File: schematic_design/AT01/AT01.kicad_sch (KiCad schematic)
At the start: 25 parts, among them J1 JST Connector, M2 Motor_DC (Pump), M3 Motor_DC (Solenoid), P1 USB_C_Plug_USB2.0, Q1 DMG2301L, SW1 SW_Push, U1 MPRLS0025PA00001A, U2 FT232RL, U3 DRV8833PW

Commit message: completed initial schematic development
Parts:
- added C7: 4.7uF, symbol Device:C
- added D2: LED, symbol Device:LED
- added J2: Conn_01x04_Pin, symbol Connector:Conn_01x04_Pin
- added R10, R5, R6, R7, R8, R9: 5.1K, symbol Device:R
- added U4: MCP73831-2-OT, Package_TO_SOT_SMD:SOT-23-5, symbol Battery_Management:MCP73831-2-OT
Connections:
- net +BATT: now also C7.2, U4.3 (V_{BAT})
- net GND: now also P1.A1 (GND), P1.A12 (GND), P1.B1 (GND), P1.B12 (GND), C7.1, D2.1 (K), R5.2, R8.2, R9.2, U4.2 (V_{SS})
- net IO32_A7: now also J2.4 (Pin_4)
- net MISO: now also J2.3 (Pin_3)
- net MOSI: now also J2.2 (Pin_2)
- net RXD0: now also U2.1 (TXD)
- net SCK: now also J2.1 (Pin_1)
- net TXD0: now also U2.5 (RXD)
- net VBUS: now also P1.A4 (VBUS), P1.A9 (VBUS), P1.B4 (VBUS), P1.B9 (VBUS), R6.1, R7.1, U4.4 (V_{DD})
- net DTR: now reaches U2.2 (DTR)
- net VBUS_UART: now reaches U2.20 (VCC), U2.4 (VCCIO)
- net VBUS_UART: now also R6.2, R7.2, R8.1
- net RTS: now reaches U2.3 (RTS)
- net at P1.A5 (CC): now also R5.1
- new net: D2.2 (A), R10.1
- new net: R10.2, U4.1 (STAT)
- new net: R9.1, U4.5 (PROG)
- no-connect marks 9 -> 18
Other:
- note added: "LIPO CHARGING CIRCUIT"
- note added: "SPI BREAKOUT HEADER"
- note added: "USB TO UART BRIDGE CIRCUIT"
- note removed: "2. add input circuit 3. add charging circuit 5. add usb to uart circuit"
- title: (none) -> AT01 - Initial Revision
- moved on the sheet: C6, P1, U2

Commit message: adding libs, cleaning up sch, initial pcb commit
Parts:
- removed R1, R2: 2.2k, symbol Device:R_Small_US
- added R12: 2.2K, Resistor_SMD:R_0402_1005Metric_Pad0.72x0.64mm_HandSolder, symbol Device:R
- added R13, R2: 10K, Resistor_SMD:R_0402_1005Metric_Pad0.72x0.64mm_HandSolder, symbol Device:R
- C1, C2, C3, C4, C5, C6, C7: footprint (none) -> Capacitor_SMD:C_01005_0402Metric_Pad0.57x0.30mm_HandSolder
- C8, C9: renamed from C?; footprint (none) -> Capacitor_SMD:C_01005_0402Metric_Pad0.57x0.30mm_HandSolder
- D2: footprint (none) -> LED_THT:LED_D3.0mm
- J1: footprint (none) -> Connector_JST:JST_EH_S2B-EH_1x02_P2.50mm_Horizontal
- J2: footprint (none) -> Connector_JST:JST_EH_S4B-EH_1x04_P2.50mm_Horizontal
- M2, M3: footprint (none) -> Connector_Samtec_HPM_THT:Samtec_HPM-02-05-x-S_Straight_1x02_Pitch5.08mm
- P1: footprint (none) -> Connector_USB:USB_C_Receptacle_Molex_105450-0101
- R10, R3, R4, R5, R6, R7, R8, R9: footprint (none) -> Resistor_SMD:R_0402_1005Metric_Pad0.72x0.64mm_HandSolder
- R11: renamed from R?; footprint (none) -> Resistor_SMD:R_0402_1005Metric_Pad0.72x0.64mm_HandSolder
- SW1: footprint (none) -> Button_Switch_THT:SW_PUSH_6mm
- gave numbers to parts that had none: 2
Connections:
- net IO27_A10 is gone; now on net DRV_SLEEP: U5.12 (IO27)
- net +3.3V: now also U1.12 (VDD), R13.1, R2.1; no longer U1.10 (VSS)
- net GND: now also C1.2, U1.10 (VSS), R12.1; no longer U3.3 (AISEN), U3.6 (BISEN)
- net SCK: now also U5.20 (SCK/CLK)
- net SCL: now also R2.2
- net SDA: now also R13.2
- net IO12_A11 renamed DRV_SLEEP
- new net: R12.2, U3.3 (AISEN), U3.6 (BISEN)
- no-connect marks 18 -> 37

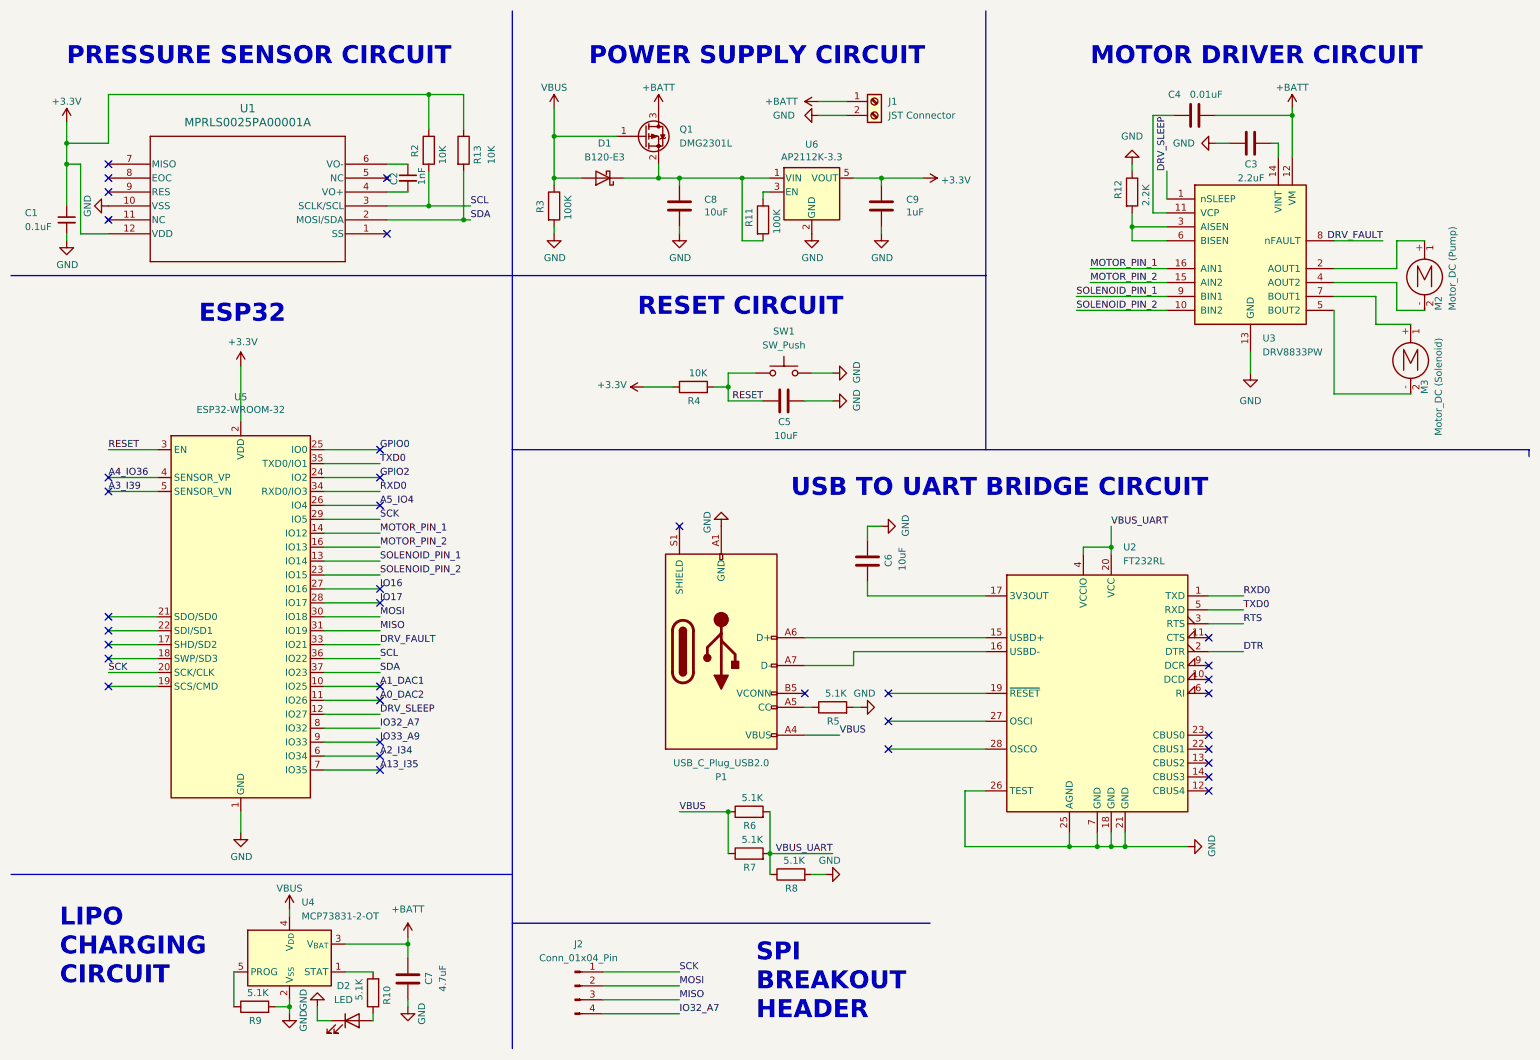
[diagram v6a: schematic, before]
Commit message: fixing up labels, gnds, added some protection diodes
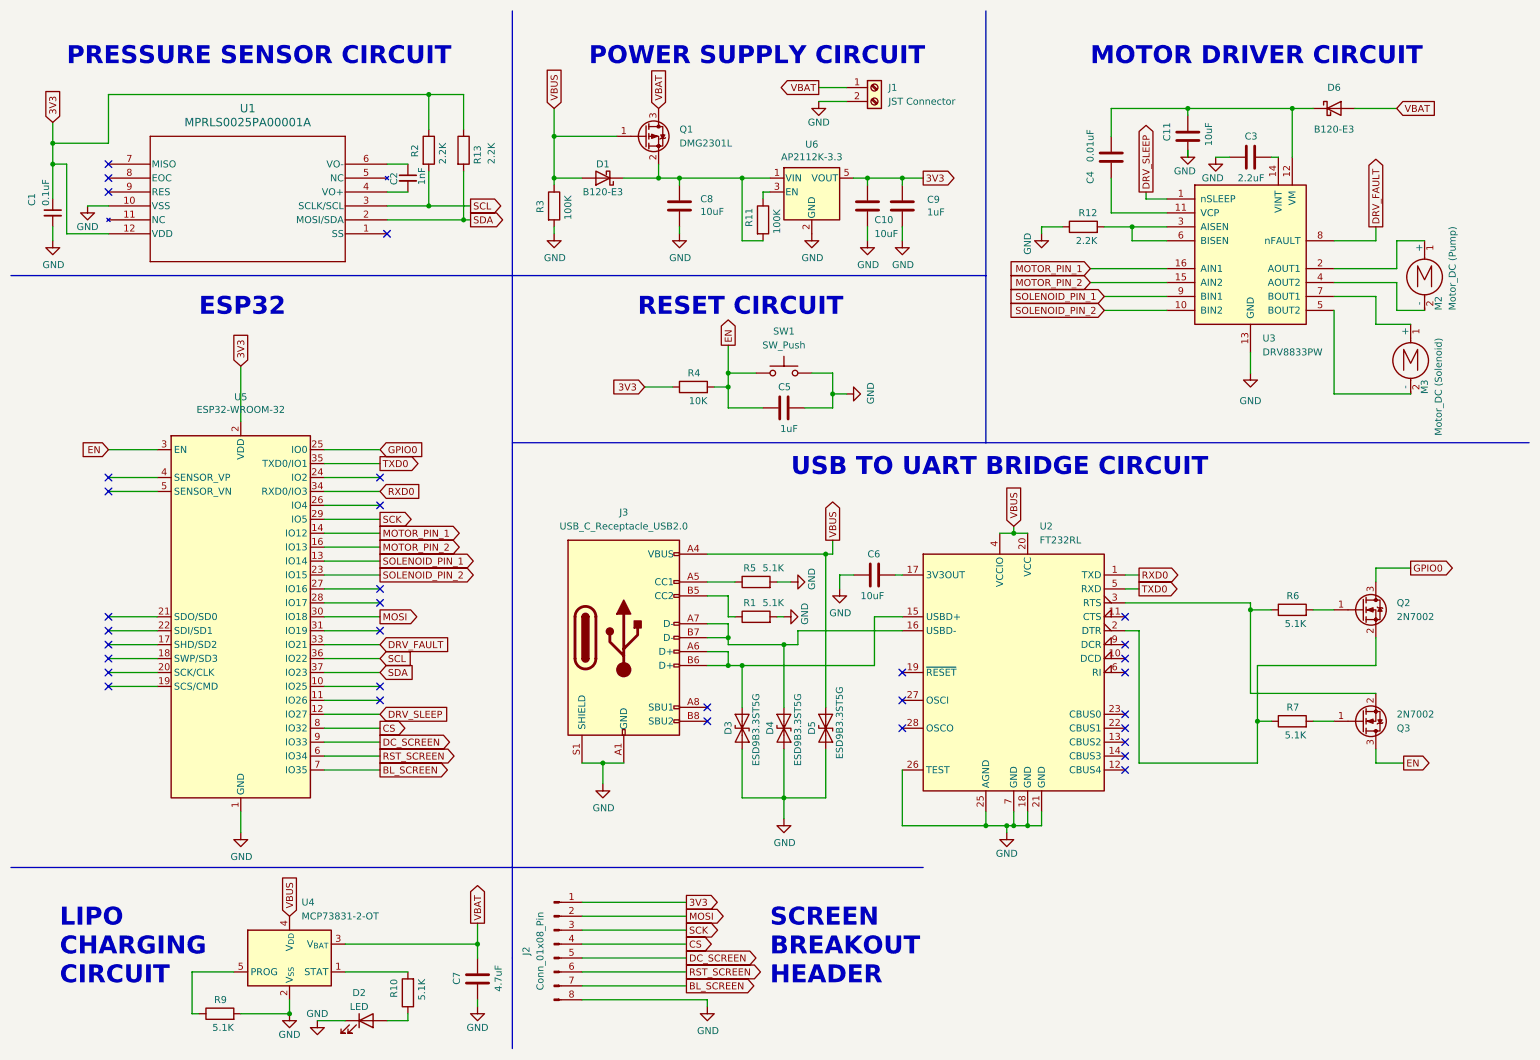
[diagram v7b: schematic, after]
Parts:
- removed J2: Conn_01x04_Pin, Connector_JST:JST_EH_S4B-EH_1x04_P2.50mm_Horizontal, symbol Connector:Conn_01x04_Pin
- removed P1: USB_C_Plug_USB2.0, Connector_USB:USB_C_Receptacle_Molex_105450-0101, symbol Connector:USB_C_Plug_USB2.0
- removed R8: 5.1K, Resistor_SMD:R_0402_1005Metric_Pad0.72x0.64mm_HandSolder, symbol Device:R
- added C10, C11: 10uF, Capacitor_SMD:C_01005_0402Metric_Pad0.57x0.30mm_HandSolder, symbol Device:C
- added D3, D4, D5: ESD9B3.3ST5G, Diode_SMD:D_SOD-923, symbol Diode:ESD9B3.3ST5G
- added D6: B120-E3, Diode_SMD:D_SMA, symbol Diode:B120-E3
- added J2: Conn_01x08_Pin, Connector_PinHeader_1.00mm:PinHeader_1x08_P1.00mm_Vertical, symbol Connector:Conn_01x08_Pin
- added J3: USB_C_Receptacle_USB2.0, Connector_USB:USB_C_Receptacle_Molex_105450-0101, symbol Connector:USB_C_Receptacle_USB2.0
- added Q2, Q3: 2N7002, Package_TO_SOT_SMD:SOT-23, symbol Transistor_FET:2N7002
- added R1: 5.1K, Resistor_SMD:R_0402_1005Metric_Pad0.72x0.64mm_HandSolder, symbol Device:R
- C5: value 10uF -> 1uF
- R13, R2: value 10K -> 2.2K
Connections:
- net GND: now also C10.2, C11.1, D3.1 (A1), D4.1 (A1), D5.1 (A1), J2.8 (Pin_8), J3.A1 (GND), J3.A12 (GND), J3.B1 (GND), J3.B12 (GND), J3.S1 (SHIELD), R1.2
- net GPIO0: now also Q2.3 (D)
- net MOSI: now also J2.2 (Pin_2)
- net SCK: now also J2.3 (Pin_3); no longer U5.20 (SCK/CLK)
- net VBUS: now also U2.20 (VCC), U2.4 (VCCIO), D5.2 (A2), J3.A4 (VBUS), J3.A9 (VBUS), J3.B4 (VBUS), J3.B9 (VBUS); no longer R6.1, R7.1
- net at U2.15 (USBD+): now also D3.2 (A2), J3.A6 (D+), J3.B6 (D+)
- net at U2.16 (USBD-): now also D4.2 (A2), J3.A7 (D-), J3.B7 (D-)
- net at R5.1: now also J3.A5 (CC1)
- net +3.3V renamed 3V3
- net 3V3: now also C10.1, J2.1 (Pin_1)
- net +BATT renamed VBAT
- net VBAT: now also D6.2 (A); no longer C4.2, U3.12 (VM)
- net A0_DAC2: no longer names the net of U5.11 (IO26)
- net A13_I35 renamed BL_SCREEN
- net BL_SCREEN: now also J2.7 (Pin_7)
- net A1_DAC1: no longer names the net of U5.10 (IO25)
- net A2_I34 renamed RST_SCREEN
- net RST_SCREEN: now also J2.6 (Pin_6)
- net A3_I39: no longer names the net of U5.5 (SENSOR_VN)
- net A4_IO36: no longer names the net of U5.4 (SENSOR_VP)
- net A5_IO4: no longer names the net of U5.26 (IO4)
- net DTR: no longer names the net of U2.2 (DTR)
- net DTR: now also R7.1, Q2.2 (S)
- net GPIO2: no longer names the net of U5.24 (IO2)
- net IO16: no longer names the net of U5.27 (IO16)
- net IO17: no longer names the net of U5.28 (IO17)
- net IO32_A7 renamed CS
- net CS: now also J2.4 (Pin_4)
- net IO33_A9 renamed DC_SCREEN
- net DC_SCREEN: now also J2.5 (Pin_5)
- net MISO: no longer names the net of U5.31 (IO19)
- net RESET renamed EN
- net EN: now also Q3.3 (D)
- net RTS: no longer names the net of U2.3 (RTS)
- net RTS: now also R6.1, Q3.2 (S)
- removed net VBUS_UART: R6.2, R7.2, U2.20 (VCC), U2.4 (VCCIO)
- new net: C11.2, C4.2, D6.1 (K), U3.12 (VM)
- new net: Q2.1 (G), R6.2
- new net: Q3.1 (G), R7.2
- new net: J3.B5 (CC2), R1.1
- no-connect marks 37 -> 33
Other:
- note added: "SCREEN BREAKOUT HEADER"
- note removed: "SPI BREAKOUT HEADER"
- moved on the sheet: C1, C3, C5, C6, C7, C9, D2, J1, R10, R12, R5, R9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

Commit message: fixing major issue with the LDO
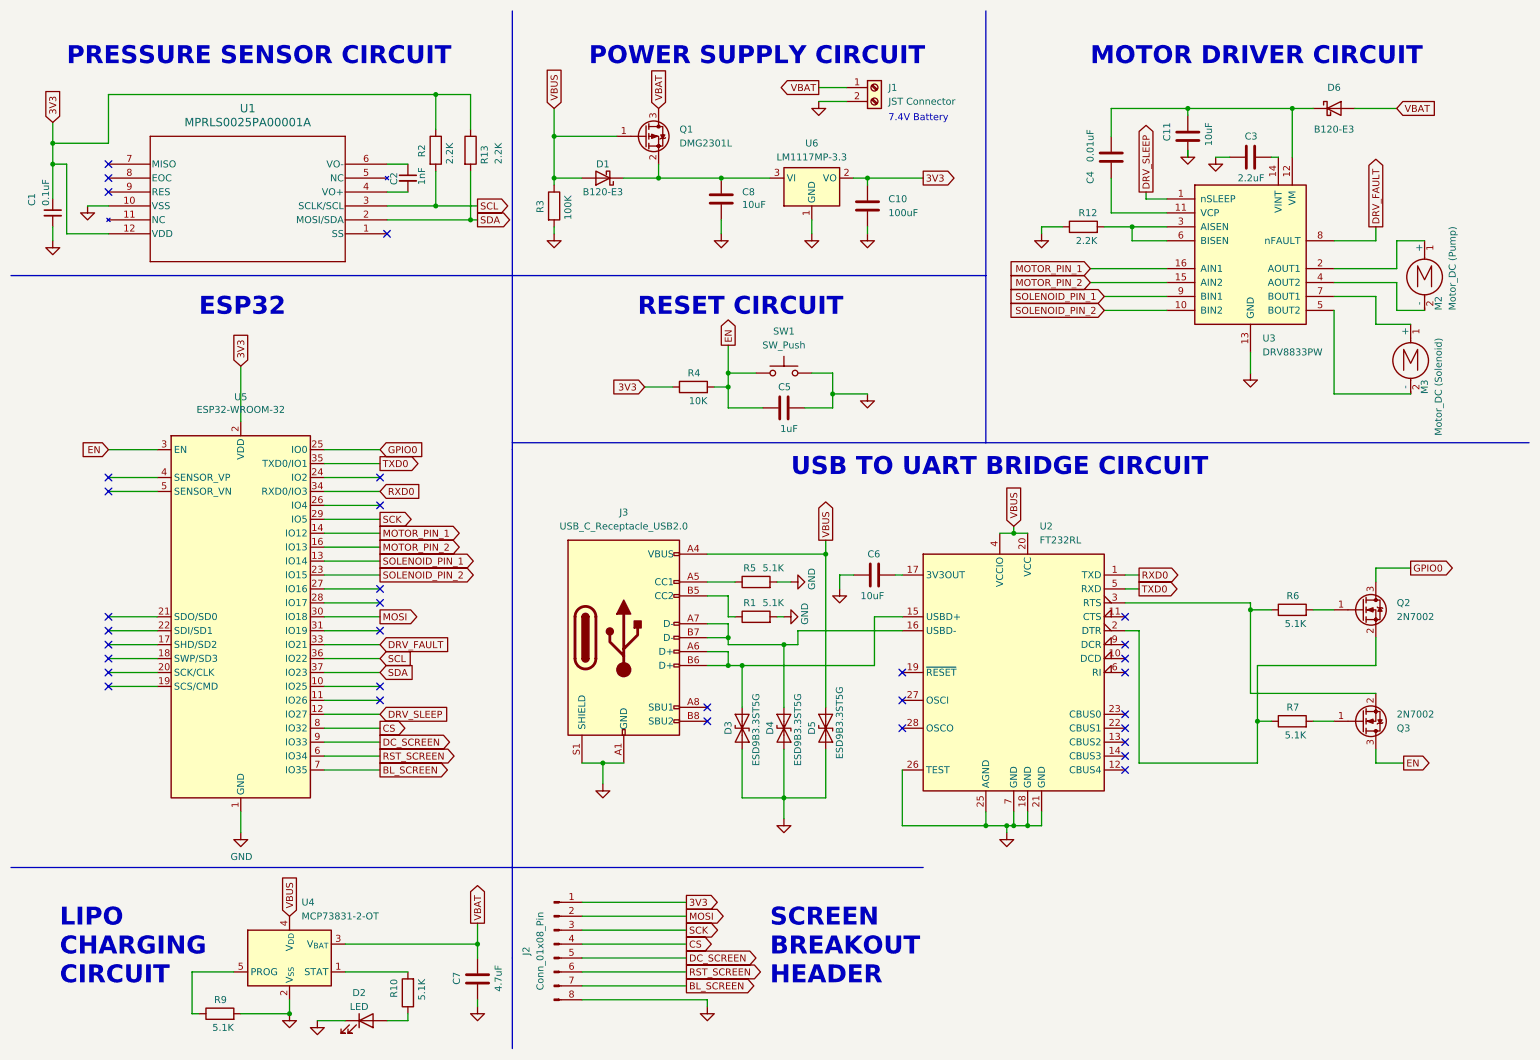
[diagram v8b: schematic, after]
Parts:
- removed C9: 1uF, Capacitor_SMD:C_01005_0402Metric_Pad0.57x0.30mm_HandSolder, symbol Device:C
- removed R11: 100K, Resistor_SMD:R_0402_1005Metric_Pad0.72x0.64mm_HandSolder, symbol Device:R
- C10: value 10uF -> 100uF
- U6: value AP2112K-3.3 -> LM1117MP-3.3; footprint Package_TO_SOT_SMD:SOT-23-5 -> Package_TO_SOT_SMD:SOT-223-3_TabPin2; symbol Regulator_Linear:AP2112K-3.3 -> Regulator_Linear:LM1117MP-3.3
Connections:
- net 3V3: now also U6.2 (VO); no longer U6.5 (VOUT)
- net GND: now also U6.1 (GND); no longer U6.2 (GND)
- net at C8.1, D1.1 (K), Q1.2 (S): now also U6.3 (VI); no longer U6.1 (VIN)
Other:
- note added: "7.4V Battery"
- title: AT01 - Initial Revision -> BP - Initial Revision
- moved on the sheet: C8, R13, R2
